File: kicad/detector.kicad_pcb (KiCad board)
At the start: 4 copper layers, 38.5 x 35.8 mm, 46 parts, among them J1 Conn_01x05_Male, J2 Conn_01x05_Male, U1 LT1761-5, U2 LT1964-5, U3 REF5010ID, U4 OPA2197xD, U5 OPA2197xD

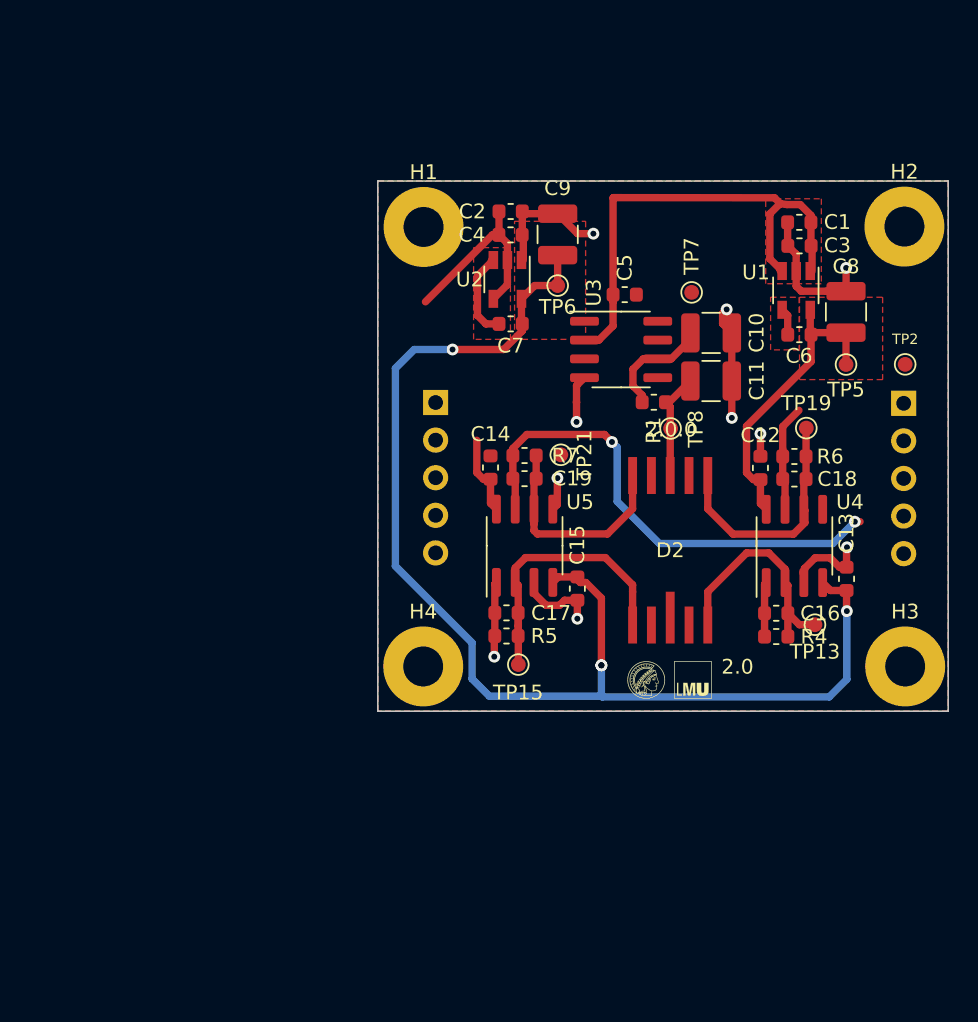
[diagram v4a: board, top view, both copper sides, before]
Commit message: redesigned detector pcb
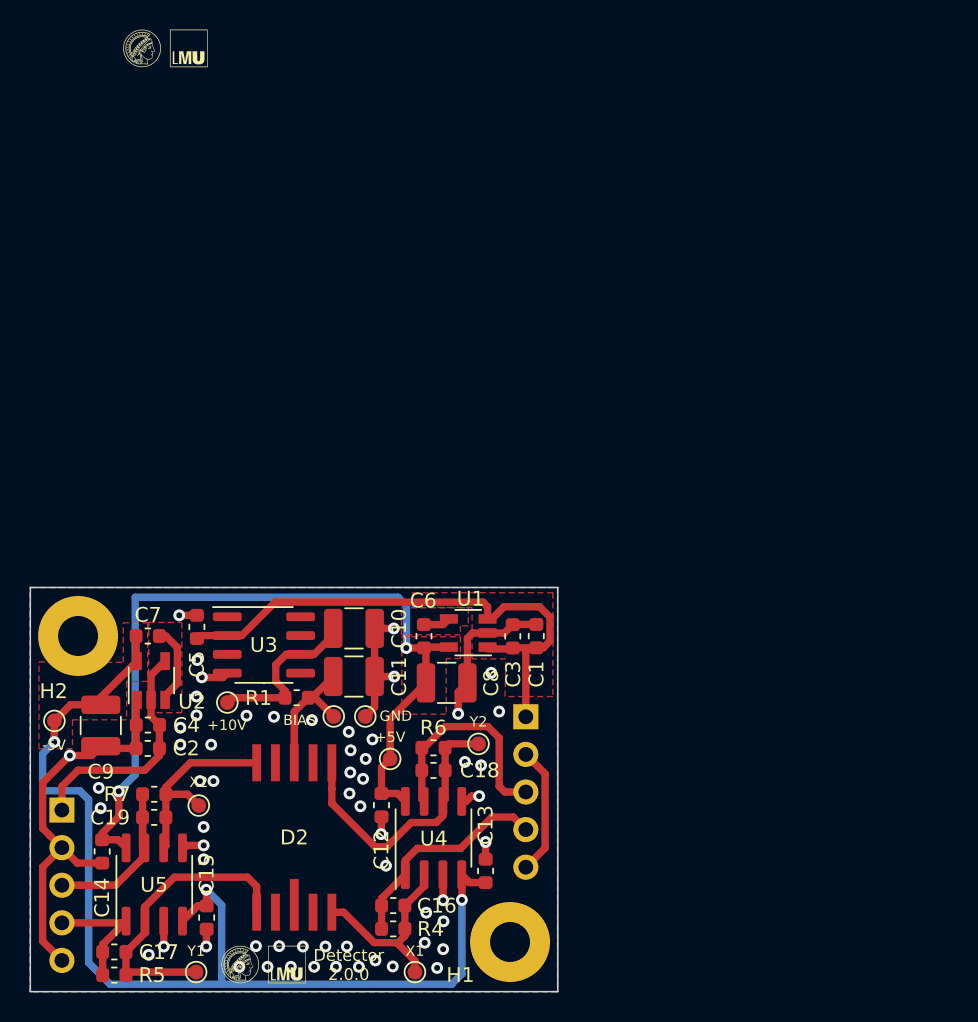
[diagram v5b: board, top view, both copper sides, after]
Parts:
- removed H3, H4: MountingHole_Pad, MountingHole:MountingHole_2.7mm_M2.5_Pad
- removed TP13: I1, TestPoint:TestPoint_Pad_D1.0mm
- removed TP15: I3, TestPoint:TestPoint_Pad_D1.0mm
- removed TP21: I2, TestPoint:TestPoint_Pad_D1.0mm
- added G***: LOGO, Common:mpq_lmu_logo, F.Cu at (137.4, 167.4)
- added X1: I1, TestPoint:TestPoint_Pad_D1.0mm, F.Cu at (147.6, 167.9)
- added X2: I2, TestPoint:TestPoint_Pad_D1.0mm, F.Cu at (133.0, 156.7)
- added Y1: I3, TestPoint:TestPoint_Pad_D1.0mm, F.Cu at (132.8, 167.9)
- moved H2 62.3 mm to (124.9, 145.2)
- moved G*** 54.6 mm to (130.8, 105.5)
- moved H1 48.7 mm to (154.1, 165.9)
- moved C9 45.3 mm to (126.4, 151.3), turned to 90 degrees
- moved -5V 45.0 mm to (123.3, 151.0), turned to 0 degrees
- moved C2 43.8 mm to (129.6, 152.8), turned to 0 degrees
- moved GND 43.5 mm to (144.3, 150.7)
- moved +10V 41.9 mm to (135.0, 149.7)
- moved C4 41.2 mm to (129.6, 151.3), turned to 0 degrees
- moved +5V 40.7 mm to (145.9, 153.5)
- moved J1 37.4 mm to (123.8, 157.0)
- moved C14 36.9 mm to (126.5, 159.8), turned to 90 degrees
- moved C8 36.8 mm to (149.8, 148.4), turned to 0 degrees
- moved C5 36.6 mm to (132.9, 144.6), turned to 90 degrees
- moved U2 36.2 mm to (129.8, 148.2), turned to 90 degrees
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- renumbered TP7 to +10V, TP5 to +5V, TP6 to -5V, TP8 to BIAS, TP2 to GND, TP19 to Y2
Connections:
- J1 pad 3: GND -> /-X2
- J1 pad 4: /-X2 -> /-Y1
- J1 pad 5: /-Y1 -> GND
- J2 pad 3: GND -> /-Y2
- J2 pad 4: /-Y2 -> /-X1
- J2 pad 5: /-X1 -> GND
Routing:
- net +5V: track 26.2 -> 56.5 mm, vias 0 -> 2
- net GND: track 43.6 -> 68.7 mm, vias 9 -> 60
- net /-X2: track 33.8 -> 12.7 mm, vias 2 -> 0
- net /-X1: track 3.69 -> 15.0 mm
- net -5V: track 84.6 -> 73.5 mm, vias 4 -> 3
- net /-Y2: track 7.21 -> 15.1 mm
- net +12V: track 33.8 -> 38.0 mm
- net Net-(C10-Pad1): track 8.51 -> 12.5 mm
- net /-Y1: track 5.08 -> 8.69 mm, vias 1 -> 0
- net Net-(C18-Pad2): track 16.3 -> 19.3 mm
- net -12V: track 13.4 -> 16.1 mm
- net Net-(C16-Pad2): track 15.8 -> 13.1 mm
- net Net-(C11-Pad1): track 7.36 -> 9.30 mm
- net Net-(C19-Pad2): track 14.8 -> 13.5 mm
- removed copper zone on In1.Cu, net GND
- removed copper zone on In2.Cu, net GND
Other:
- board size 38.5 x 35.8 mm -> 35.6 x 27.3 mm
- copper layers 4 -> 2
- board text added: "Detector 2.0.0"
- board text removed: "2.0"
- board text removed: "2.0.0"

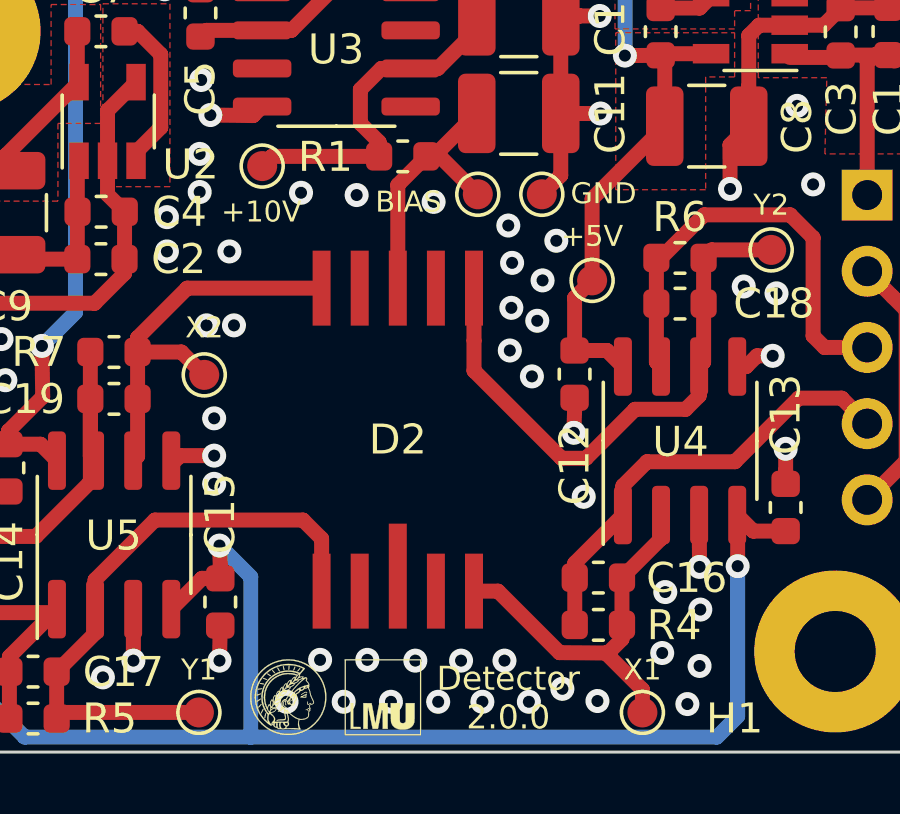
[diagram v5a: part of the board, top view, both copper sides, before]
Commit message: removed some vias from detector pcb
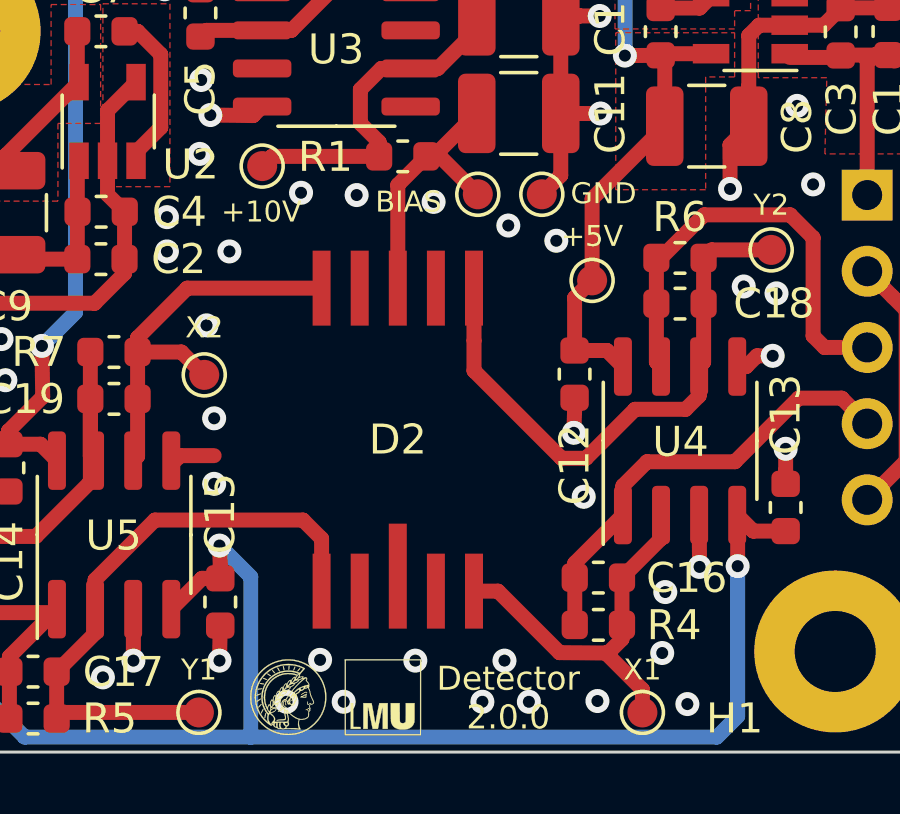
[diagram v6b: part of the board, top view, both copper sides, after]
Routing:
- net GND: vias 60 -> 44
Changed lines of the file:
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@@
     (thickness 1.6)
     (drawings 5)
-    (tracks 327)
+    (tracks 311)
     (zones 0)
     (modules 45)
@@
   (segment (start 132.2168 159.385) (end 133.35 159.385) (width 0.5) (layer F.Cu) (net 1))
   (segment (start 133.35 159.385) (end 133.35 159.385) (width 0.5) (layer F.Cu) (net 1))
-  (via (at 133.35 159.385) (size 0.8) (drill 0.4) (layers F.Cu B.Cu) (net 1))
   (segment (start 130.6498 164.5016) (end 130.6498 164.635) (width 0.5) (layer F.Cu) (net 1))
   (segment (start 130.6498 164.635) (end 130.6576 164.6428) (width 0.5) (layer F.Cu) (net 1))
@@
   (via (at 138.0998 150.6982) (size 0.8) (drill 0.4) (layers F.Cu B.Cu) (net 1))
   (via (at 136.2456 150.622) (size 0.8) (drill 0.4) (layers F.Cu B.Cu) (net 1))
-  (via (at 132.8674 150.5966) (size 0.8) (drill 0.4) (layers F.Cu B.Cu) (net 1))
   (via (at 133.858 152.5778) (size 0.8) (drill 0.4) (layers F.Cu B.Cu) (net 1))
   (via (at 131.7752 152.5778) (size 0.8) (drill 0.4) (layers F.Cu B.Cu) (net 1))
   (via (at 133.096 155.0416) (size 0.8) (drill 0.4) (layers F.Cu B.Cu) (net 1))
-  (via (at 134.0104 155.0416) (size 0.8) (drill 0.4) (layers F.Cu B.Cu) (net 1))
   (via (at 126.2634 155.4988) (size 0.8) (drill 0.4) (layers F.Cu B.Cu) (net 1))
   (via (at 126.3904 156.8704) (size 0.8) (drill 0.4) (layers F.Cu B.Cu) (net 1))
@@
   (via (at 148.3868 163.9316) (size 0.8) (drill 0.4) (layers F.Cu B.Cu) (net 1))
   (via (at 148.2852 165.9636) (size 0.8) (drill 0.4) (layers F.Cu B.Cu) (net 1))
-  (via (at 149.5552 164.5158) (size 0.8) (drill 0.4) (layers F.Cu B.Cu) (net 1))
-  (via (at 149.5298 166.3954) (size 0.8) (drill 0.4) (layers F.Cu B.Cu) (net 1))
   (via (at 143.0274 166.2176) (size 0.8) (drill 0.4) (layers F.Cu B.Cu) (net 1))
-  (via (at 141.5796 166.2176) (size 0.8) (drill 0.4) (layers F.Cu B.Cu) (net 1))
-  (via (at 140.0556 166.2176) (size 0.8) (drill 0.4) (layers F.Cu B.Cu) (net 1))
-  (via (at 138.4554 166.1922) (size 0.8) (drill 0.4) (layers F.Cu B.Cu) (net 1))
   (via (at 136.8806 166.1922) (size 0.8) (drill 0.4) (layers F.Cu B.Cu) (net 1))
   (via (at 135.763 167.5892) (size 0.8) (drill 0.4) (layers F.Cu B.Cu) (net 1))
   (via (at 137.668 167.5892) (size 0.8) (drill 0.4) (layers F.Cu B.Cu) (net 1))
-  (via (at 139.2428 167.5892) (size 0.8) (drill 0.4) (layers F.Cu B.Cu) (net 1))
-  (via (at 140.8176 167.5892) (size 0.8) (drill 0.4) (layers F.Cu B.Cu) (net 1))
   (via (at 142.2908 167.5892) (size 0.8) (drill 0.4) (layers F.Cu B.Cu) (net 1))
   (via (at 143.8402 167.5892) (size 0.8) (drill 0.4) (layers F.Cu B.Cu) (net 1))
   (via (at 146.1262 167.5638) (size 0.8) (drill 0.4) (layers F.Cu B.Cu) (net 1))
-  (via (at 144.9578 167.1574) (size 0.8) (drill 0.4) (layers F.Cu B.Cu) (net 1))
   (via (at 133.35 158.1404) (size 0.8) (drill 0.4) (layers F.Cu B.Cu) (net 1))
   (via (at 133.35 160.3248) (size 0.8) (drill 0.4) (layers F.Cu B.Cu) (net 1))
@@
   (via (at 144.7546 152.2222) (size 0.8) (drill 0.4) (layers F.Cu B.Cu) (net 1))
   (via (at 143.1544 151.7142) (size 0.8) (drill 0.4) (layers F.Cu B.Cu) (net 1))
-  (via (at 143.9418 156.7434) (size 0.8) (drill 0.4) (layers F.Cu B.Cu) (net 1))
-  (via (at 143.2052 155.8798) (size 0.8) (drill 0.4) (layers F.Cu B.Cu) (net 1))
-  (via (at 144.1196 154.8892) (size 0.8) (drill 0.4) (layers F.Cu B.Cu) (net 1))
-  (via (at 144.2974 153.543) (size 0.8) (drill 0.4) (layers F.Cu B.Cu) (net 1))
-  (via (at 143.2814 152.9588) (size 0.8) (drill 0.4) (layers F.Cu B.Cu) (net 1))
-  (via (at 143.256 154.4574) (size 0.8) (drill 0.4) (layers F.Cu B.Cu) (net 1))
   (via (at 132.8674 149.3266) (size 0.8) (drill 0.4) (layers F.Cu B.Cu) (net 1))
   (via (at 132.9182 146.8628) (size 0.8) (drill 0.4) (layers F.Cu B.Cu) (net 1))
@@
   (segment (start 156.417801 159.558199) (end 156.417801 154.538201) (width 0.5) (layer F.Cu) (net 1))
   (segment (start 155.1178 160.8582) (end 156.417801 159.558199) (width 0.5) (layer F.Cu) (net 1))
+  (via (at 140.0556 166.2176) (size 0.8) (drill 0.4) (layers F.Cu B.Cu) (net 1))
   (segment (start 149.5352 144.4655) (end 149.9141 144.0866) (width 0.5) (layer F.Cu) (net 2))
   (segment (start 148.2341 144.4655) (end 149.5352 144.4655) (width 0.5) (layer F.Cu) (net 2))

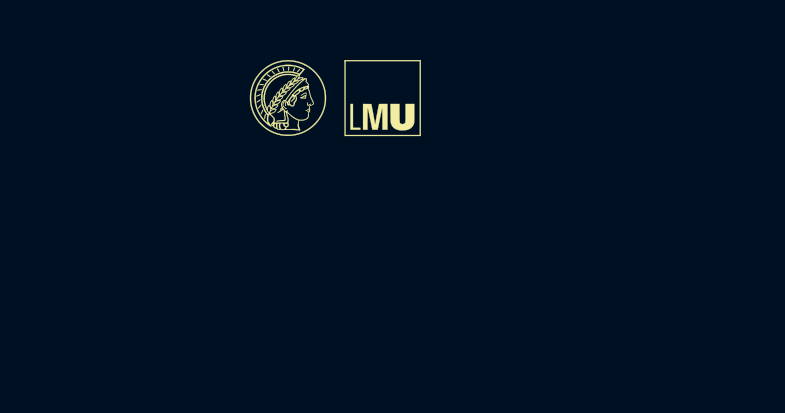
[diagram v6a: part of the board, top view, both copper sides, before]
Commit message: adjusted arithmetic pcb for updated detector pcb
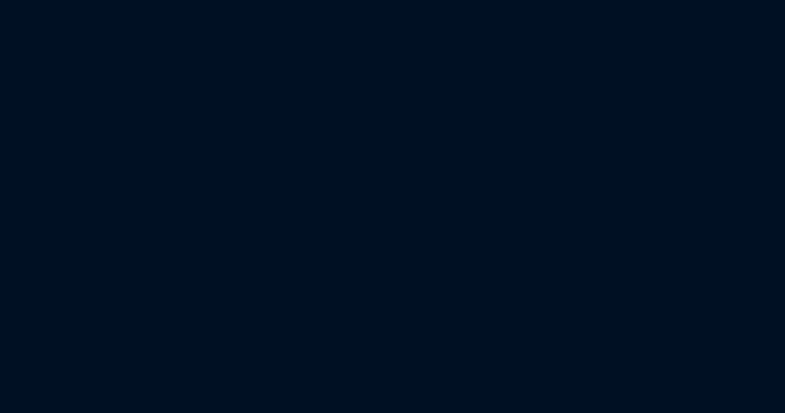
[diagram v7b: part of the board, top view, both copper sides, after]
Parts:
- removed the G*** at (130.8, 105.5)

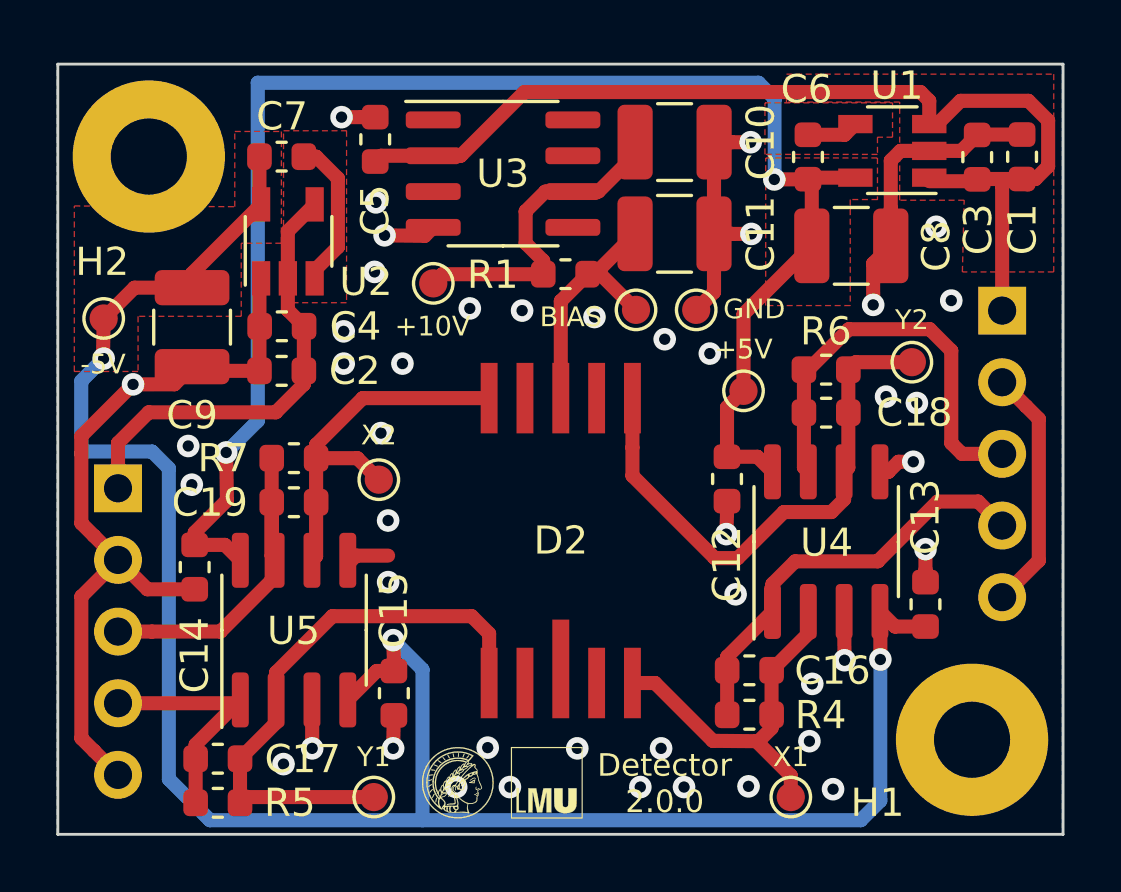
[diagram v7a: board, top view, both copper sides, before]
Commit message: fix some DRC errors, remove some test points
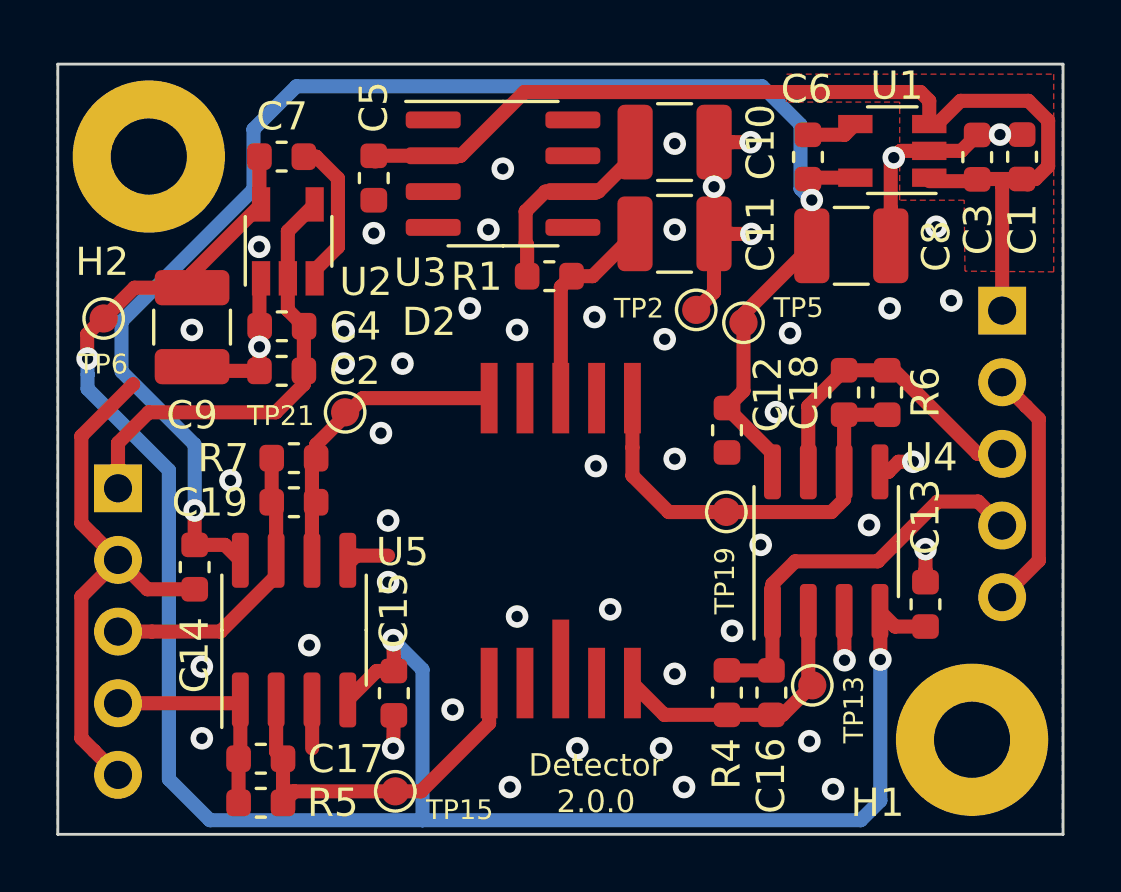
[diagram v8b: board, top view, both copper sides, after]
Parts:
- removed +10V: +10V, TestPoint:TestPoint_Pad_D1.0mm
- removed BIAS: BIAS, TestPoint:TestPoint_Pad_D1.0mm
- removed G***: LOGO, Common:mpq_lmu_logo
- moved TP19 8.45 mm to (145.3, 157.8), turned to 180 degrees
- moved TP13 4.04 mm to (148.4, 164.0), turned to 90 degrees
- moved TP21 2.67 mm to (131.8, 154.3)
- moved TP5 2.41 mm to (145.9, 151.1), turned to 90 degrees
- moved R6 2.31 mm to (151.0, 153.6), turned to 270 degrees
- moved C12 1.73 mm to (145.4, 154.9)
- moved C17 1.52 mm to (128.8, 166.6)
- moved R5 1.52 mm to (128.8, 168.1)
- moved C5 1.37 mm to (132.8, 146.0), turned to 270 degrees
- moved R4 1.12 mm to (145.4, 164.2), turned to 270 degrees
- moved C16 1.11 mm to (146.9, 164.2), turned to 270 degrees
- moved C18 0.96 mm to (149.5, 153.6), turned to 270 degrees
- moved TP15 0.79 mm to (133.6, 167.7)
- moved R1 0.58 mm to (139.1, 149.5)
- renumbered X1 to TP13, Y1 to TP15, Y2 to TP19, GND to TP2, X2 to TP21, +5V to TP5, -5V to TP6
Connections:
- H2 pad 1: GND -> (no net)
- U3 pad 1: Net-(U3-Pad1) -> (no net)
- U3 pad 3: Net-(U3-Pad3) -> (no net)
- U3 pad 5: Net-(U3-Pad5) -> (no net)
- U3 pad 7: Net-(U3-Pad7) -> (no net)
- U3 pad 8: Net-(U3-Pad8) -> (no net)
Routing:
- net GND: track 68.7 -> 59.7 mm, vias 44 -> 51
- net Net-(C17-Pad2): track 20.4 -> 14.1 mm
- net Net-(C10-Pad1): track 12.5 -> 8.35 mm
- net /-Y2: track 15.1 -> 11.0 mm
- net Net-(C18-Pad2): track 19.3 -> 15.5 mm
- net Net-(C16-Pad2): track 13.1 -> 9.95 mm
- net Net-(C19-Pad2): track 13.5 -> 11.0 mm
- net /-X2: track 12.7 -> 10.7 mm
- net Net-(C11-Pad1): track 9.30 -> 7.35 mm
- net -5V: track 73.5 -> 71.7 mm
- net /-Y1: track 8.69 -> 7.72 mm
- net /-X1: track 15.0 -> 14.4 mm
- net +5V: track 56.5 -> 57.0 mm
- removed copper zone on F.Cu, net +5V
- removed copper zone on F.Cu, net -5V
- removed copper zone on F.Cu, net Net-(C6-Pad1)
- removed copper zone on F.Cu, net Net-(C7-Pad2)
